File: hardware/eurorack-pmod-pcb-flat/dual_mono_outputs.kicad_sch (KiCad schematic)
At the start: 13 parts, among them J10 PJ398SM, J9 PJ398SM, U6 TL074, U7 TL074

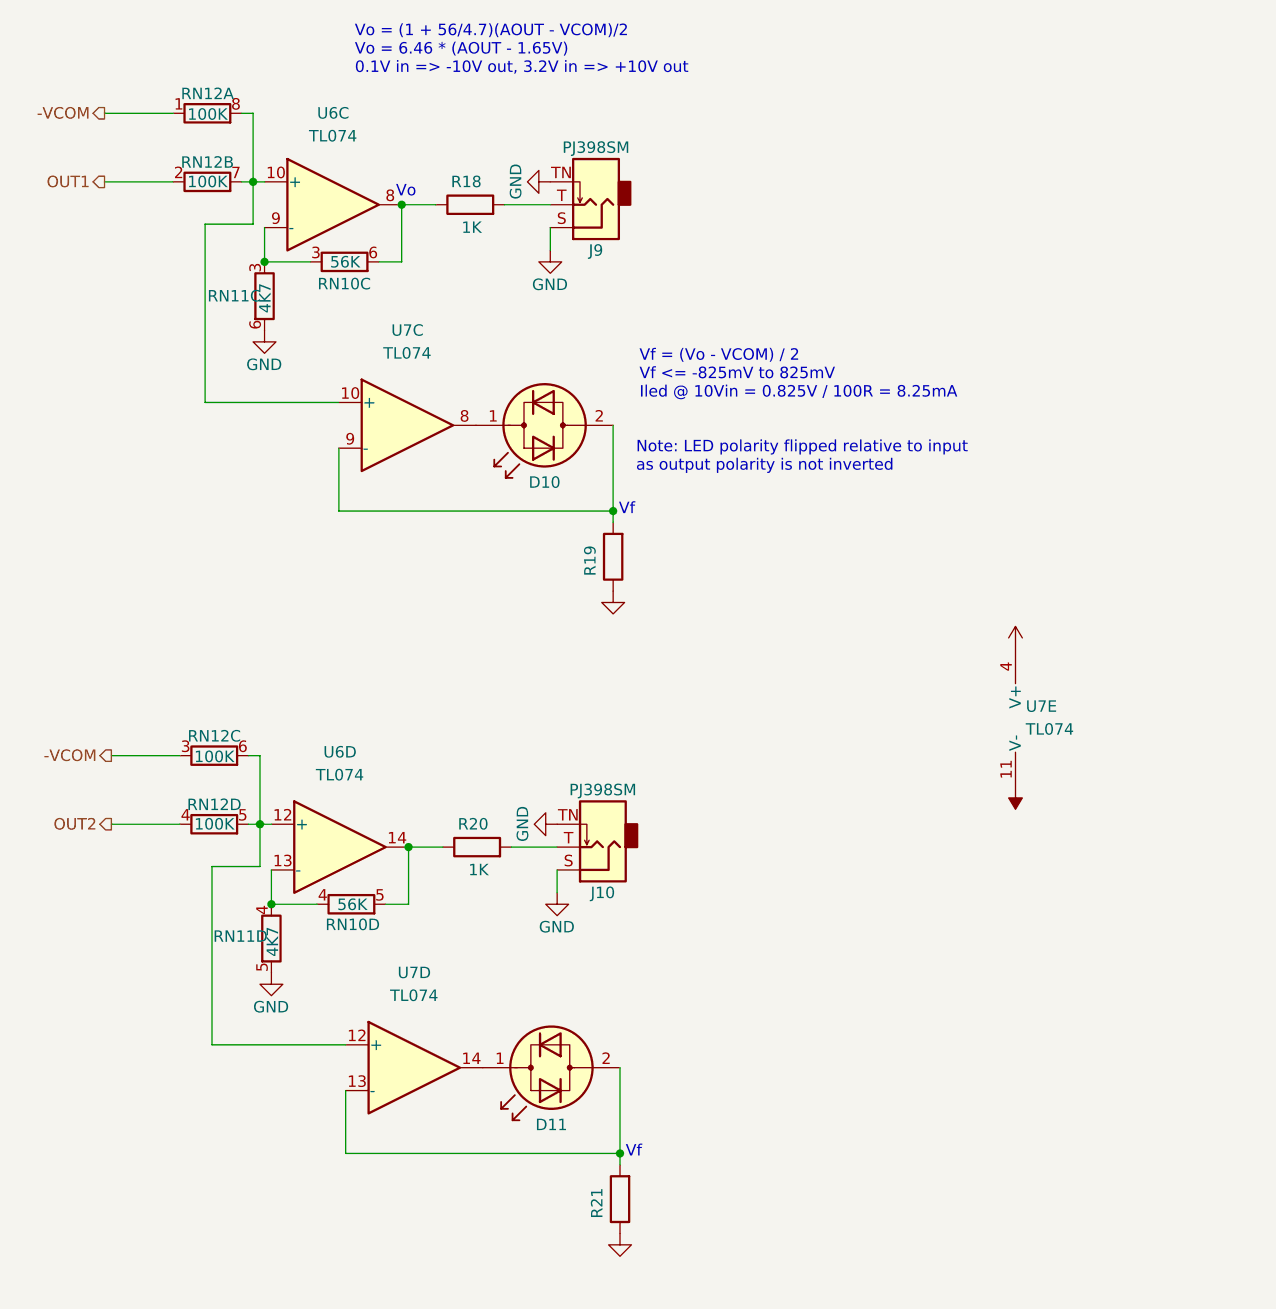
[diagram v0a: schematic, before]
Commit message: rev2-flat: add vref and stabilization caps
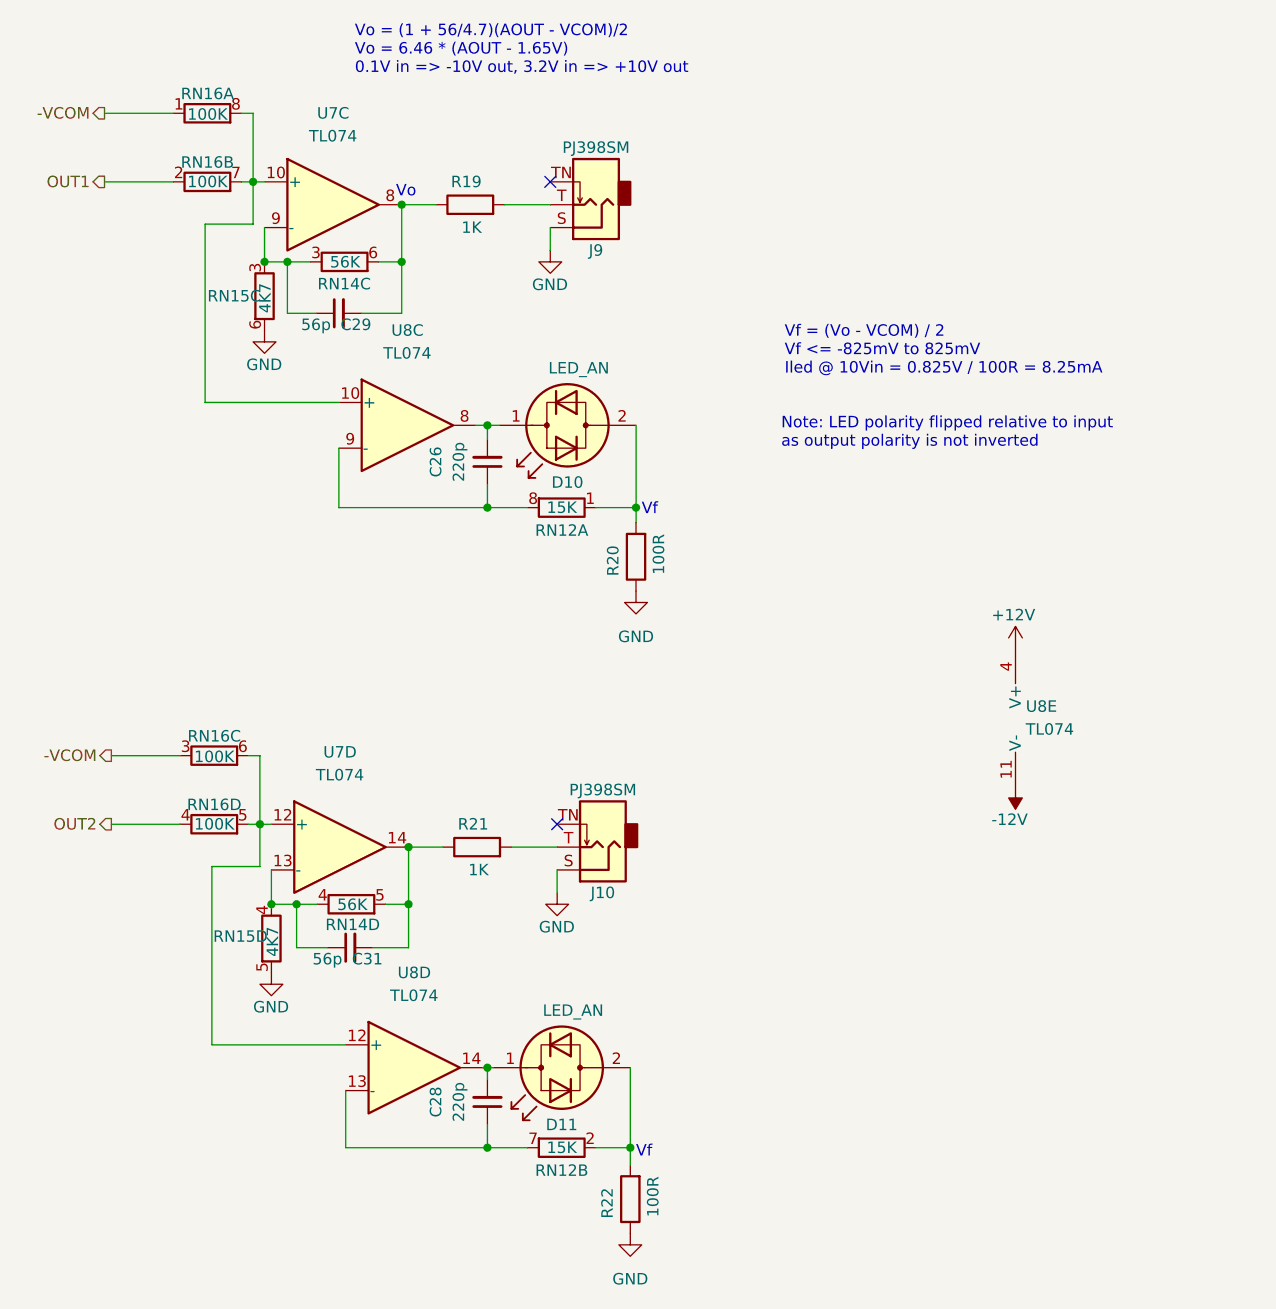
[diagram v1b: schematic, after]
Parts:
- added C26, C28: 220p, Capacitor_SMD:C_0603_1608Metric, symbol Device:C_Small
- added C29, C31: 56p, Capacitor_SMD:C_0603_1608Metric, symbol Device:C_Small
- added RN12: 15K, Resistor_SMD:R_Cat16-4, symbol Device:R_Pack04_Split
- D10, D11: value (none) -> LED_AN
- R20: renamed from R19; value (none) -> 100R
- R22: renamed from R21; value (none) -> 100R
- renumbered R18 to R19, R20 to R21, RN10 to RN14, RN11 to RN15, RN12 to RN16, U6 to U7, U7 to U8
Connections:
- net GND: no longer J10.TN, J9.TN
- net at RN14.3 (R3.1), RN15.3 (R3.1), U7.9 (-): now also C29.1
- net at D10.1 (KA), U8.8: now also C26.2
- net at D10.2 (AK), R20.2: now also RN12.1 (R1.1); no longer U8.9 (-)
- net at R19.1, RN14.6 (R3.2), U7.8: now also C29.2
- net at RN14.4 (R4.1), RN15.4 (R4.1), U7.13 (-): now also C31.1
- net at R21.1, RN14.5 (R4.2), U7.14: now also C31.2
- net at D11.2 (AK), R22.2: now also RN12.2 (R2.1); no longer U8.13 (-)
- net at D11.1 (KA), U8.14: now also C28.2
- new net: C28.1, RN12.7 (R2.2), U8.13 (-)
- new net: C26.1, RN12.8 (R1.2), U8.9 (-)
- no-connect marks 0 -> 2
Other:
- moved on the sheet: D10, D11, R20, R22

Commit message: rev2-flat: update power supply and add bypass electros
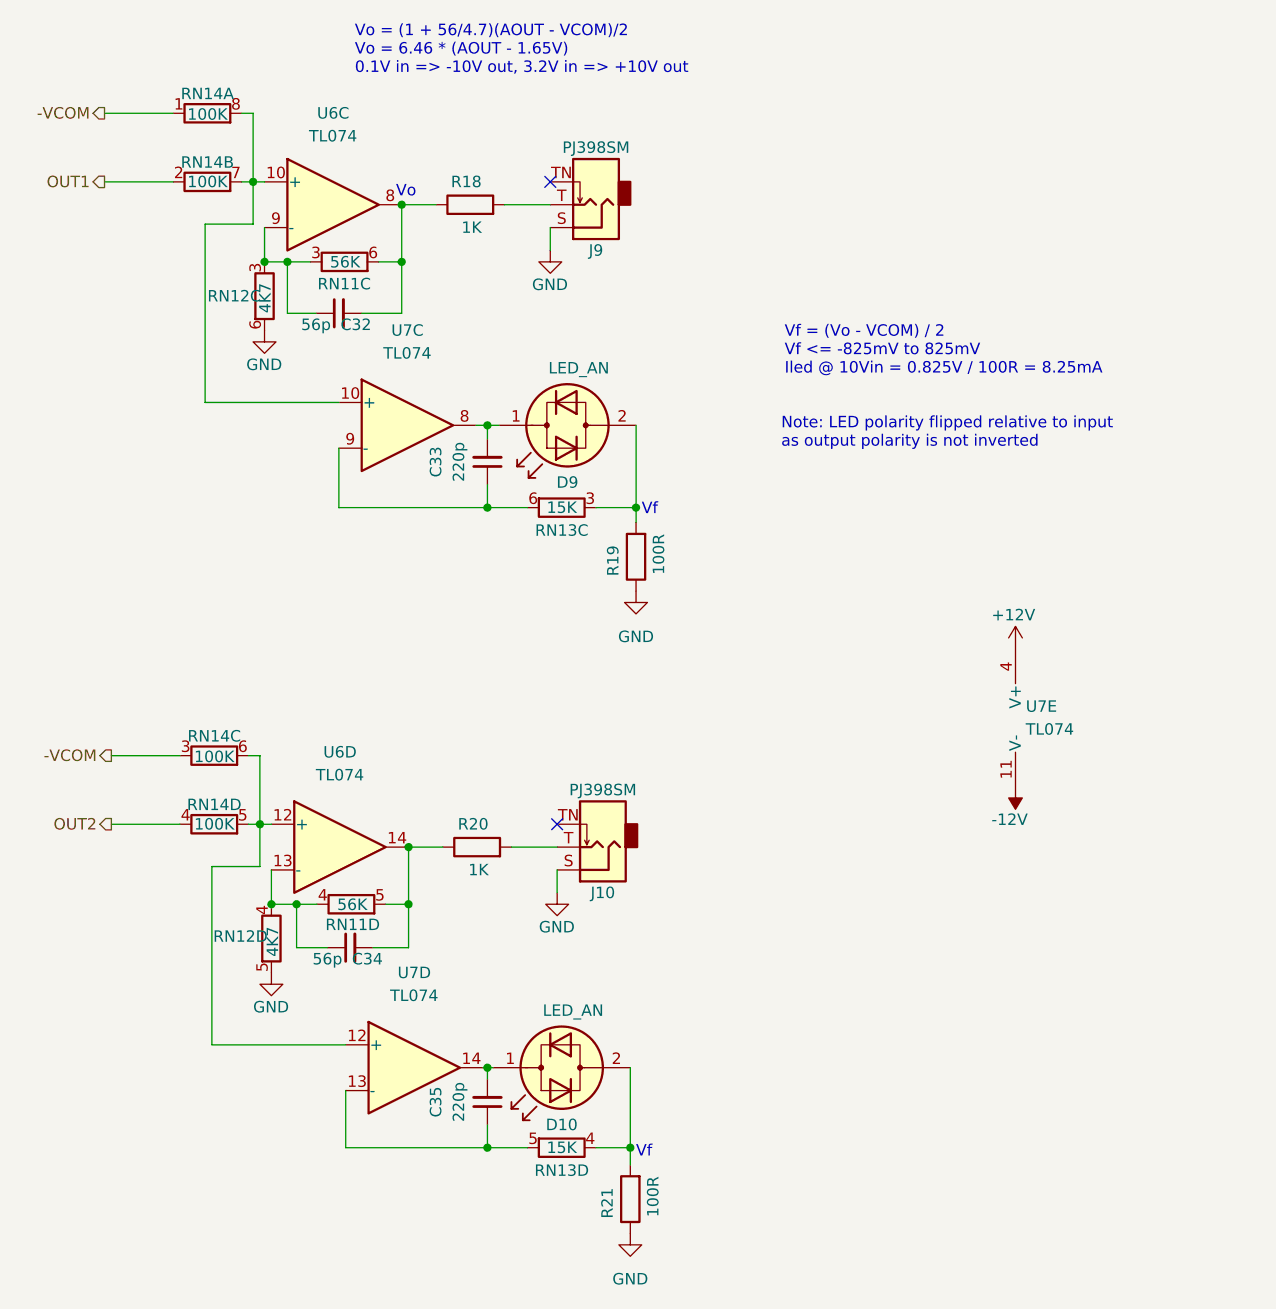
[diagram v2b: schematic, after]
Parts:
- renumbered C29 to C32, C26 to C33, C31 to C34, C28 to C35, D11 to D10, D10 to D9, R19 to R18, R20 to R19, R21 to R20, R22 to R21, RN14 to RN11, RN15 to RN12, RN12 to RN13, RN16 to RN14, U7 to U6, U8 to U7
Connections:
- net at D9.2 (AK), R19.2: now also RN13.3 (R3.1); no longer RN13.1 (R1.1)
- net at C35.1, U7.13 (-): now also RN13.5 (R4.2); no longer RN13.7 (R2.2)
- net at D10.2 (AK), R21.2: now also RN13.4 (R4.1); no longer RN13.2 (R2.1)
- net at C33.1, U7.9 (-): now also RN13.6 (R3.2); no longer RN13.8 (R1.2)

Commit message: rev2-flat: update fields and fab1 export
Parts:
- RN11: dig# (none) -> CAT16-563J4LFCT-ND; mfg# (none) -> CAT16-563J4LF
- RN12: dig# (none) -> CAT16-4701F4LFCT-ND; mfg# (none) -> CAT16-472F4LF
- RN13: dig# CAY16-1502F4LFCT-ND -> CAT16-1502F4LFCT-ND; mfg# CAY16-1502F4LF -> CAT16-1502F4LF
- RN14: dig# CAY16-1003F4LFCT-ND -> CAT16-1003F4LFCT-ND; mfg# CAY16-1003F4LF -> CAT16-1003F4LF
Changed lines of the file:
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@@
       (effects (font (size 1.27 1.27)) hide)
     )
-    (property "dig#" "CAY16-1003F4LFCT-ND" (id 4) (at 36.322 106.934 0)
-      (effects (font (size 1.27 1.27)) hide)
-    )
-    (property "mfg#" "CAY16-1003F4LF" (id 5) (at 36.322 106.934 0)
+    (property "dig#" "CAT16-1003F4LFCT-ND" (id 4) (at 36.322 106.934 0)
+      (effects (font (size 1.27 1.27)) hide)
+    )
+    (property "mfg#" "CAT16-1003F4LF" (id 5) (at 36.322 106.934 0)
       (effects (font (size 1.27 1.27)) hide)
     )
@@
       (effects (font (size 1.27 1.27)) hide)
     )
-    (property "dig#" "CAY16-1003F4LFCT-ND" (id 4) (at 36.322 114.554 0)
-      (effects (font (size 1.27 1.27)) hide)
-    )
-    (property "mfg#" "CAY16-1003F4LF" (id 5) (at 36.322 114.554 0)
+    (property "dig#" "CAT16-1003F4LFCT-ND" (id 4) (at 36.322 114.554 0)
+      (effects (font (size 1.27 1.27)) hide)
+    )
+    (property "mfg#" "CAT16-1003F4LF" (id 5) (at 36.322 114.554 0)
       (effects (font (size 1.27 1.27)) hide)
     )
@@
       (effects (font (size 1.27 1.27)) hide)
     )
-    (property "dig#" "CAY16-1003F4LFCT-ND" (id 4) (at 35.56 43.18 0)
-      (effects (font (size 1.27 1.27)) hide)
-    )
-    (property "mfg#" "CAY16-1003F4LF" (id 5) (at 35.56 43.18 0)
+    (property "dig#" "CAT16-1003F4LFCT-ND" (id 4) (at 35.56 43.18 0)
+      (effects (font (size 1.27 1.27)) hide)
+    )
+    (property "mfg#" "CAT16-1003F4LF" (id 5) (at 35.56 43.18 0)
       (effects (font (size 1.27 1.27)) hide)
     )
@@
     )
     (property "Datasheet" "~" (id 3) (at 41.91 55.88 0)
+      (effects (font (size 1.27 1.27)) hide)
+    )
+    (property "dig#" "CAT16-4701F4LFCT-ND" (id 4) (at 41.91 55.88 0)
+      (effects (font (size 1.27 1.27)) hide)
+    )
+    (property "mfg#" "CAT16-472F4LF" (id 5) (at 41.91 55.88 0)
       (effects (font (size 1.27 1.27)) hide)
     )
@@
       (effects (font (size 1.27 1.27)) hide)
     )
+    (property "dig#" "CAT16-4701F4LFCT-ND" (id 4) (at 42.672 127.254 0)
+      (effects (font (size 1.27 1.27)) hide)
+    )
+    (property "mfg#" "CAT16-472F4LF" (id 5) (at 42.672 127.254 0)
+      (effects (font (size 1.27 1.27)) hide)
+    )
     (pin "1")
     (pin "8")
@@
       (effects (font (size 1.27 1.27)) hide)
     )
+    (property "dig#" "CAT16-563J4LFCT-ND" (id 4) (at 50.8 52.07 0)
+      (effects (font (size 1.27 1.27)) hide)
+    )
+    (property "mfg#" "CAT16-563J4LF" (id 5) (at 50.8 52.07 0)
+      (effects (font (size 1.27 1.27)) hide)
+    )
     (pin "1")
     (pin "8")
@@
     )
     (property "Datasheet" "~" (id 3) (at 51.562 123.444 0)
+      (effects (font (size 1.27 1.27)) hide)
+    )
+    (property "dig#" "CAT16-563J4LFCT-ND" (id 4) (at 51.562 123.444 0)
+      (effects (font (size 1.27 1.27)) hide)
+    )
+    (property "mfg#" "CAT16-563J4LF" (id 5) (at 51.562 123.444 0)
       (effects (font (size 1.27 1.27)) hide)
     )
@@
       (effects (font (size 1.27 1.27)) hide)
     )
-    (property "dig#" "CAY16-1003F4LFCT-ND" (id 4) (at 35.56 35.56 0)
-      (effects (font (size 1.27 1.27)) hide)
-    )
-    (property "mfg#" "CAY16-1003F4LF" (id 5) (at 35.56 35.56 0)
+    (property "dig#" "CAT16-1003F4LFCT-ND" (id 4) (at 35.56 35.56 0)
+      (effects (font (size 1.27 1.27)) hide)
+    )
+    (property "mfg#" "CAT16-1003F4LF" (id 5) (at 35.56 35.56 0)
       (effects (font (size 1.27 1.27)) hide)
     )
@@
       (effects (font (size 1.27 1.27)) hide)
     )
-    (property "dig#" "CAY16-1502F4LFCT-ND" (id 4) (at 74.93 79.375 0)
-      (effects (font (size 1.27 1.27)) hide)
-    )
-    (property "mfg#" "CAY16-1502F4LF" (id 5) (at 74.93 79.375 0)
+    (property "dig#" "CAT16-1502F4LFCT-ND" (id 4) (at 74.93 79.375 0)
+      (effects (font (size 1.27 1.27)) hide)
+    )
+    (property "mfg#" "CAT16-1502F4LF" (id 5) (at 74.93 79.375 0)
       (effects (font (size 1.27 1.27)) hide)
     )
@@
       (effects (font (size 1.27 1.27)) hide)
     )
-    (property "dig#" "CAY16-1502F4LFCT-ND" (id 4) (at 74.93 150.495 0)
-      (effects (font (size 1.27 1.27)) hide)
-    )
-    (property "mfg#" "CAY16-1502F4LF" (id 5) (at 74.93 150.495 0)
-      (effects (font (size 1.27 1.27)) hide)
-    )
+    (property "dig#" "CAT16-1502F4LFCT-ND" (id 4) (at 74.93 150.495 0)
+      (effects (font (size 1.27 1.27)) hide)
+    )
+    (property "mfg#" "CAT16-1502F4LF" (id 5) (at 74.93 150.495 0)
+      (effects (font (size 1.27 1.27)) hide)
+    )
